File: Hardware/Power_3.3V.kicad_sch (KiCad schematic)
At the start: 12 parts, among them U5 PTPSM863253RDXR

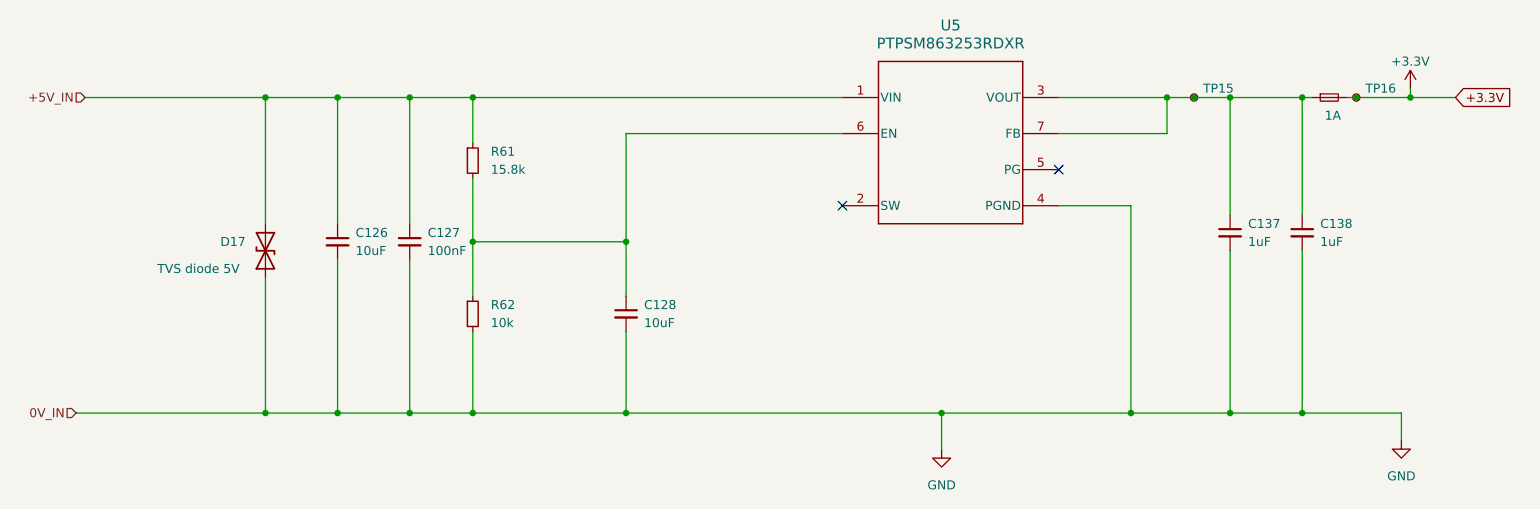
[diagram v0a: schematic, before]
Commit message: Bms plug and play, 2nd iteration with the same pinout
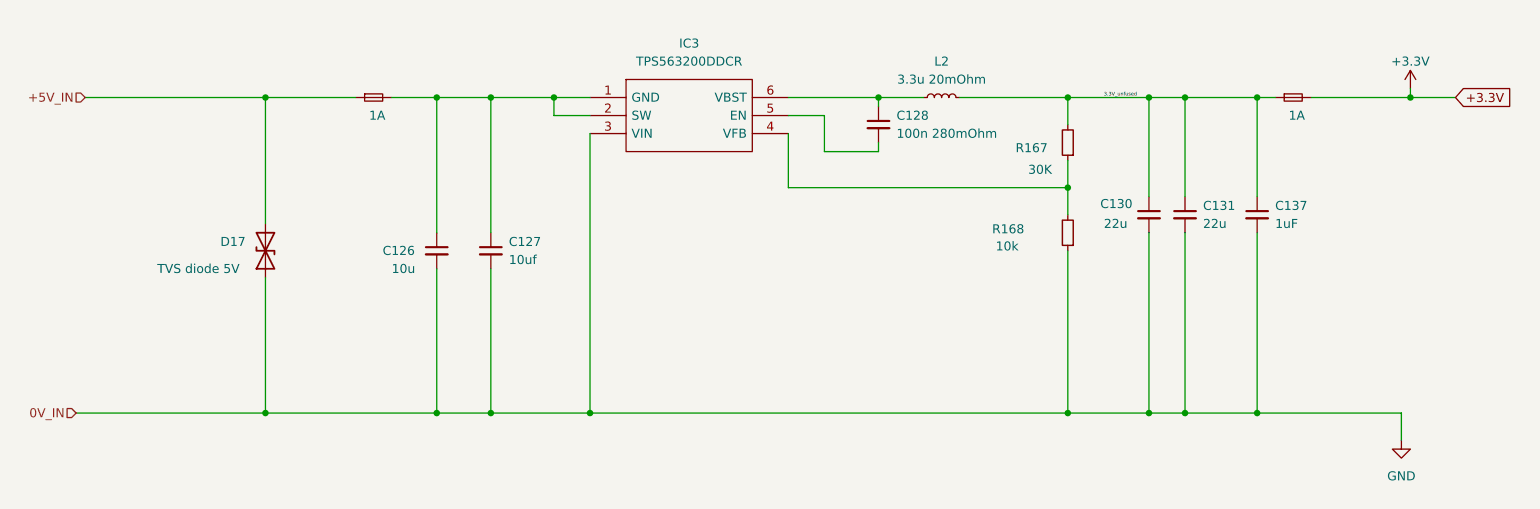
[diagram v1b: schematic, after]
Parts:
- removed C138: 1uF, Capacitor_SMD:C_0603_1608Metric_Pad1.08x0.95mm_HandSolder, symbol Device:C_Small
- removed R61: 15.8k, Resistor_SMD:R_0603_1608Metric_Pad0.98x0.95mm_HandSolder, symbol Device:R_Small
- removed R62: 10k, Resistor_SMD:R_0603_1608Metric_Pad0.98x0.95mm_HandSolder, symbol Device:R_Small
- removed TP15, TP16: TestPoint_Small, TestPoint:TestPoint_Pad_D1.0mm, symbol Connector:TestPoint_Small
- removed U5: PTPSM863253RDXR, footrpint:RDX0007A-MFG_NOVIA, symbol RDX0007A-MFG:PTPSM863253RDXR
- added C130, C131: 22u, Capacitor_SMD:C_0603_1608Metric_Pad1.08x0.95mm_HandSolder, symbol Device:C_Small
- added F39: 1A, Fuse:Fuse_1206_3216Metric, symbol Device:Fuse_Small
- added IC3: TPS563200DDCR, Package_TO_SOT_SMD:SOT-23-6, symbol TPS563200DDCR:TPS563200DDCR
- added L2: 3.3u 20mOhm, footrpint:CLF7045__, symbol Device:L_Small
- added R167: 30K, Resistor_SMD:R_0603_1608Metric, symbol Device:R_Small
- added R168: 10k, Resistor_SMD:R_0603_1608Metric, symbol Device:R_Small
- C126: value 10uF -> 10u; footprint Capacitor_SMD:C_0603_1608Metric_Pad1.08x0.95mm_HandSolder -> Capacitor_SMD:C_0805_2012Metric_Pad1.18x1.45mm_HandSolder; Field5 10uF 3mOhm -> (none)
- C127: value 100nF -> 10uf; footprint Capacitor_SMD:C_0603_1608Metric_Pad1.08x0.95mm_HandSolder -> Capacitor_SMD:C_0805_2012Metric_Pad1.18x1.45mm_HandSolder; Field5 100nF 280mOhm -> (none)
- C128: value 10uF -> 100n 280mOhm; footprint Capacitor_SMD:C_0603_1608Metric_Pad1.08x0.95mm_HandSolder -> Capacitor_SMD:C_0805_2012Metric_Pad1.18x1.45mm_HandSolder; Field5 10uF 3mOhm -> (none)
- F5: footprint Fuse:Fuse_0603_1608Metric_Pad1.05x0.95mm_HandSolder -> Fuse:Fuse_1206_3216Metric
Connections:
- net +5V_IN: now also F39.1; no longer C126.1, C127.1
- net GND: now also C130.2, C131.2, IC3.3 (VIN), R168.1; no longer C128.2
- net 3.3V_unfused: now reaches C137.1, F5.1
- net 3.3V_unfused: now also C130.1, C131.1, L2.2, R167.2
- net at C128.1: now also IC3.6 (VBST), L2.1
- new net: C126.1, C127.1, F39.2, IC3.1 (GND), IC3.2 (SW)
- new net: IC3.4 (VFB), R167.1, R168.2
- new net: C128.2, IC3.5 (EN)
- no-connect marks 2 -> 0

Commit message: New connectors jst_xh for low voltage side of bms
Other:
- title: (none) -> Battery Management System for a high power gokart battery
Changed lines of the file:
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@@
 	(generator_version "10.0")
 	(paper "A4")
+	(title_block
+		(title "Battery Management System for a high power gokart battery")
+	)
 	(junction
 		(at 215.9 120.65)

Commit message: No drc errors
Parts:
- removed C126: 10u, Capacitor_SMD:C_0805_2012Metric_Pad1.18x1.45mm_HandSolder, symbol Device:C_Small
- removed C127: 10uf, Capacitor_SMD:C_0805_2012Metric_Pad1.18x1.45mm_HandSolder, symbol Device:C_Small
- removed C128: 100n 280mOhm, Capacitor_SMD:C_0805_2012Metric_Pad1.18x1.45mm_HandSolder, symbol Device:C_Small
- added C122: 100n 280mOhm, Capacitor_SMD:C_0603_1608Metric, symbol Device:C_Small
- added C160, C161: 22u, Capacitor_SMD:C_0805_2012Metric, symbol Device:C_Small
- added R179: 10k, Resistor_SMD:R_0603_1608Metric, symbol Device:R_Small
- C130, C131: footprint Capacitor_SMD:C_0603_1608Metric_Pad1.08x0.95mm_HandSolder -> Capacitor_SMD:C_0805_2012Metric
- C137: footprint Capacitor_SMD:C_0603_1608Metric_Pad1.08x0.95mm_HandSolder -> Resistor_SMD:R_0603_1608Metric
- D17: value TVS diode 5V -> P6SMB6.8CA/TR13; footprint Diode_SMD:D_SOD-323_HandSoldering -> Diode_SMD:D_SMB
- L2: value 3.3u 20mOhm -> 3.3u; footprint footrpint:CLF7045__ -> Inductor_SMD:L_Sunlord_MWSA0402S
- R167: value 30K -> 33.2
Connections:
- net GND: now also IC3.1 (GND), C160.2, C161.2; no longer IC3.3 (VIN)
- net at L2.1: now also IC3.2 (SW), C122.2; no longer IC3.6 (VBST)
- net at IC3.5 (EN): now also R179.1
- new net: C122.1, IC3.6 (VBST)
- new net: C160.1, C161.1, F39.2, IC3.3 (VIN), R179.2
